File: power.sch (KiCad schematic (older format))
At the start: 9 parts

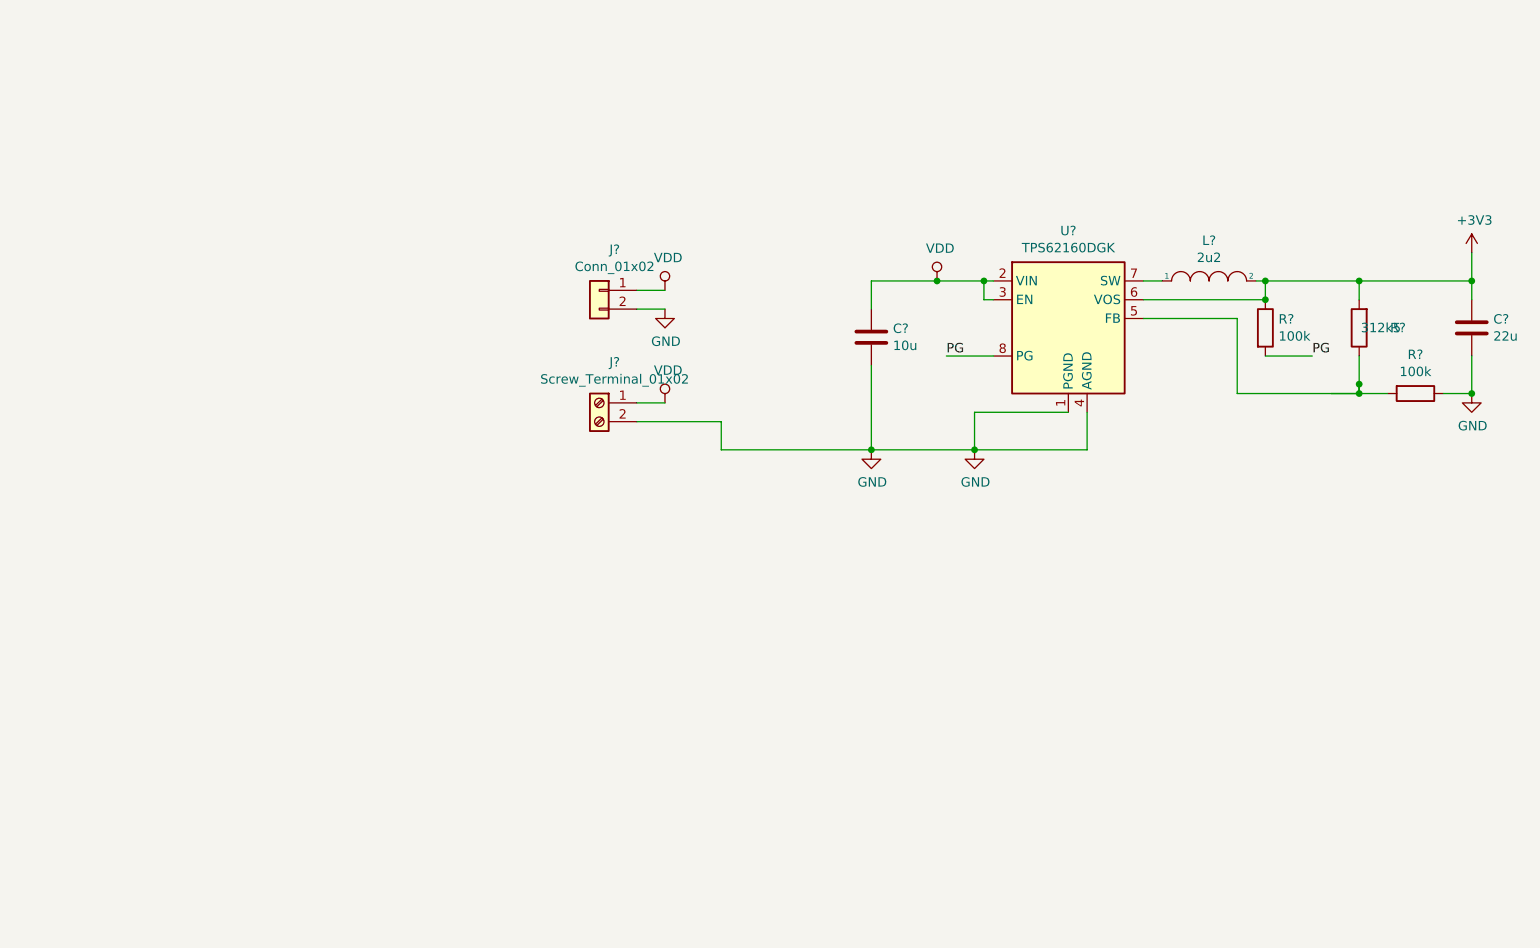
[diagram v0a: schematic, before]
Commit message: Added 12v and 5v  power supply
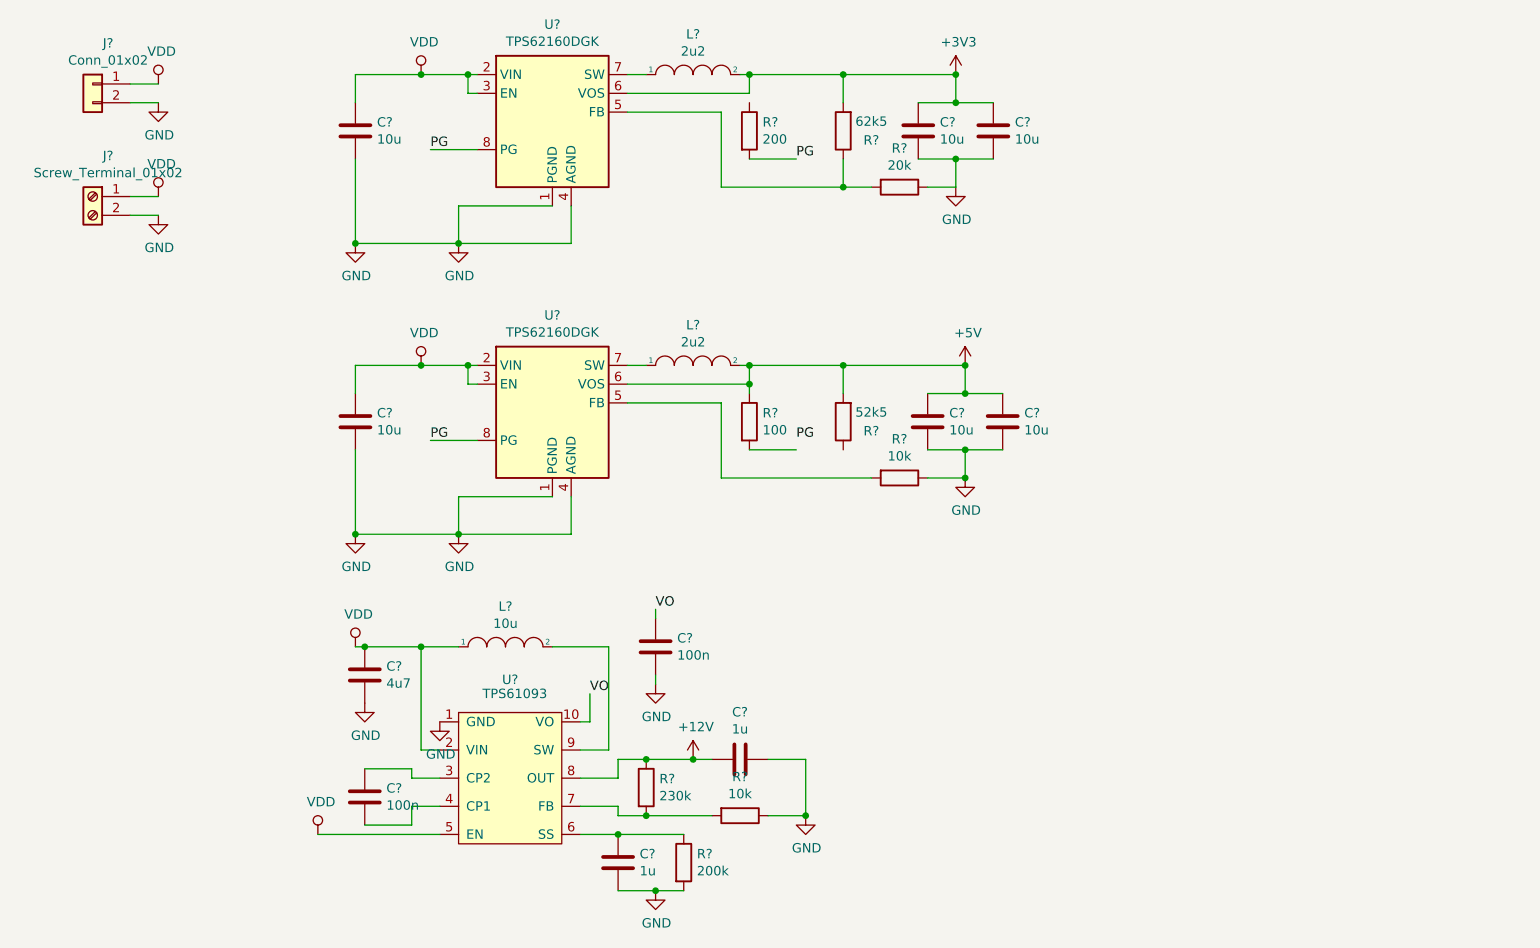
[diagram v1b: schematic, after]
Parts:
- removed C?: 22u, Capacitor_SMD:C_0201_0603Metric, symbol Device:C
- added C? (x5): 10u, Capacitor_SMD:CP_Elec_4x5.4, symbol Device:C
- added C? (x2): 100n, Capacitor_SMD:C_0603_1608Metric, symbol Device:C
- added C?: 4u7, Capacitor_SMD:C_0603_1608Metric, symbol Device:C
- added C? (x2): 1u, Capacitor_SMD:C_0603_1608Metric, symbol Device:C
- added L?: 2u2, symbol pspice:INDUCTOR
- added L?: 10u, symbol pspice:INDUCTOR
- added R? (x2): 10k, Resistor_SMD:R_0603_1608Metric, symbol Device:R
- added R?: 100, Resistor_SMD:R_0603_1608Metric, symbol Device:R
- added R?: 52k5, Resistor_SMD:R_0603_1608Metric, symbol Device:R
- added R?: 200k, Resistor_SMD:R_0603_1608Metric, symbol Device:R
- added R?: 230k, Resistor_SMD:R_0603_1608Metric, symbol Device:R
- added U?: TPS62160DGK, Package_SO:MSOP-8_3x3mm_P0.65mm, symbol Regulator_Switching:TPS62160DGK
- added U?: TPS61093, symbol iclr:TPS61093
- C?: footprint Capacitor_SMD:C_0201_0603Metric -> Capacitor_SMD:CP_Elec_4x5.4
- R?: value 100k -> 20k
- R?: value 312k5 -> 62k5
- R?: value 100k -> 200
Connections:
- net labels added: +12V, +5V, VO
- wire segments 39 -> 104
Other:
- moved on the sheet: C?, J?, L?, R?, U?

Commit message: Merge remote-tracking branch 'origin/master'
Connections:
- net +3V3: now also C?.1, C?.1, L?.1, U?.2 (VIN), U?.2 (VIN), U?.3 (EN)
- net VDD: no longer C?.1, C?.1, L?.1, U?.2 (VIN), U?.2 (VIN), U?.3 (EN)
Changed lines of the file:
@@
 EESchema Schematic File Version 4
-LIBS:daq-hardware-cache
 EELAYER 30 0
 EELAYER END
 $Descr A4 11693 8268
 encoding utf-8
-Sheet 3 5
+Sheet 1 1
 Title ""
 Date ""
@@
 	1    0    0    -1
 $EndComp
-$Comp
-L power:VDD #PWR?
-U 1 1 5DAB5D87
-P 2800 1200
-F 0 "#PWR?" H 2800 1050 50  0001 C CNN
-F 1 "VDD" H 2817 1373 50  0000 C CNN
-F 2 "" H 2800 1200 50  0001 C CNN
-F 3 "" H 2800 1200 50  0001 C CNN
-	1    2800 1200
-	1    0    0    -1
-$EndComp
-Wire Wire Line
-	2800 1200 3050 1200
 Wire Wire Line
 	3050 1200 3050 1300
@@
 $EndComp
 Wire Wire Line
-	2800 1200 2450 1200
-Wire Wire Line
 	2450 1200 2450 1350
-Connection ~ 2800 1200
 $Comp
 L power:GND #PWR?
@@
 	1    0    0    -1
 $EndComp
-$Comp
-L power:VDD #PWR?
-U 1 1 5DB05F62
-P 2800 2750
-F 0 "#PWR?" H 2800 2600 50  0001 C CNN
-F 1 "VDD" H 2817 2923 50  0000 C CNN
-F 2 "" H 2800 2750 50  0001 C CNN
-F 3 "" H 2800 2750 50  0001 C CNN
-	1    2800 2750
-	1    0    0    -1
-$EndComp
-Wire Wire Line
-	2800 2750 3050 2750
 Wire Wire Line
 	3050 2750 3050 2850
@@
 $EndComp
 Wire Wire Line
-	2800 2750 2450 2750
-Wire Wire Line
 	2450 2750 2450 2900
-Connection ~ 2800 2750
 $Comp
 L power:GND #PWR?
@@
 $Comp
 L power:VDD #PWR?
-U 1 1 5DBC3A47
-P 2450 4250
-F 0 "#PWR?" H 2450 4100 50  0001 C CNN
-F 1 "VDD" H 2467 4423 50  0000 C CNN
-F 2 "" H 2450 4250 50  0001 C CNN
-F 3 "" H 2450 4250 50  0001 C CNN
-	1    2450 4250
-	1    0    0    -1
-$EndComp
-$Comp
-L power:VDD #PWR?
 U 1 1 5DBC98EF
 P 2250 5250
@@
 	1    0    0    -1
 $EndComp
+Wire Wire Line
+	2450 2750 3050 2750
+Wire Wire Line
+	2450 1200 3050 1200
+$Comp
+L power:+3V3 #PWR?
+U 1 1 5DB9D618
+P 2450 2750
+F 0 "#PWR?" H 2450 2600 50  0001 C CNN
+F 1 "+3V3" H 2465 2923 50  0000 C CNN
+F 2 "" H 2450 2750 50  0001 C CNN
+F 3 "" H 2450 2750 50  0001 C CNN
+	1    2450 2750
+	1    0    0    -1
+$EndComp
+Connection ~ 2450 2750
+$Comp
+L power:+3V3 #PWR?
+U 1 1 5DBA6E0E
+P 2450 4250
+F 0 "#PWR?" H 2450 4100 50  0001 C CNN
+F 1 "+3V3" H 2465 4423 50  0000 C CNN
+F 2 "" H 2450 4250 50  0001 C CNN
+F 3 "" H 2450 4250 50  0001 C CNN
+	1    2450 4250
+	1    0    0    -1
+$EndComp
+$Comp
+L power:VDD #PWR?
+U 1 1 5DBA9D40
+P 2450 1200
+F 0 "#PWR?" H 2450 1050 50  0001 C CNN
+F 1 "VDD" H 2467 1373 50  0000 C CNN
+F 2 "" H 2450 1200 50  0001 C CNN
+F 3 "" H 2450 1200 50  0001 C CNN
+	1    2450 1200
+	1    0    0    -1
+$EndComp
+Connection ~ 2450 1200
 $EndSCHEMATC
